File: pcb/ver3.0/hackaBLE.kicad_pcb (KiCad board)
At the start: 2 copper layers, 20.3 x 29.9 mm, 32 parts, among them J1 GPIO, J2 GPIO, J3 GPIO, J5 GPIO, J7 SWD, SW1 SW_Push, U1 nrf52832, U3 RF_Antenna, Y1 32.768KHz, Y2 32MHz

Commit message: still working on it alot of error still there.
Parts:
- moved C3 6.82 mm to (169.2, 123.4), turned to 90 degrees
- moved C4 4.31 mm to (169.2, 127.5), turned to -90 degrees
- moved SW1 4.17 mm to (180.2, 128.2)
- moved R1 2.36 mm to (174.2, 129.5)
- moved R3 1.45 mm to (180.4, 125.8)
- moved R2 1.35 mm to (180.4, 124.2)
- moved R4 1.25 mm to (180.4, 122.8)
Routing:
- net VDD: track 77.6 -> 68.1 mm
- net GND: track 55.5 -> 60.7 mm
- net /RESET: track 33.2 -> 29.3 mm
- net /GREEN: track 15.2 -> 13.2 mm
- net /P0.09: track 25.1 -> 26.2 mm
- net /BLUE: track 13.8 -> 12.6 mm
- net /P0.10: track 27.3 -> 28.2 mm
- net /RED: track 13.3 -> 13.9 mm
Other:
- board size 20.3 x 29.9 mm -> 24.2 x 29.9 mm

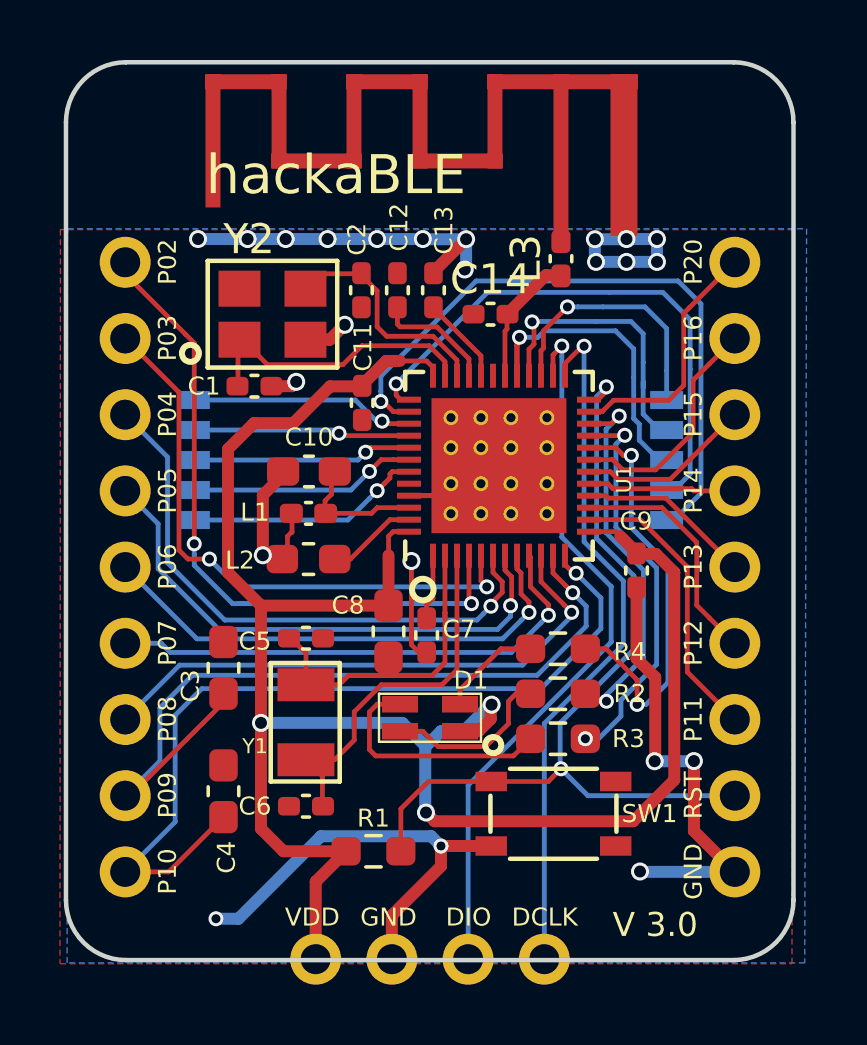
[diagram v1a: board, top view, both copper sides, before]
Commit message: now Version 3.0 has no Error and ready for manufacturing.
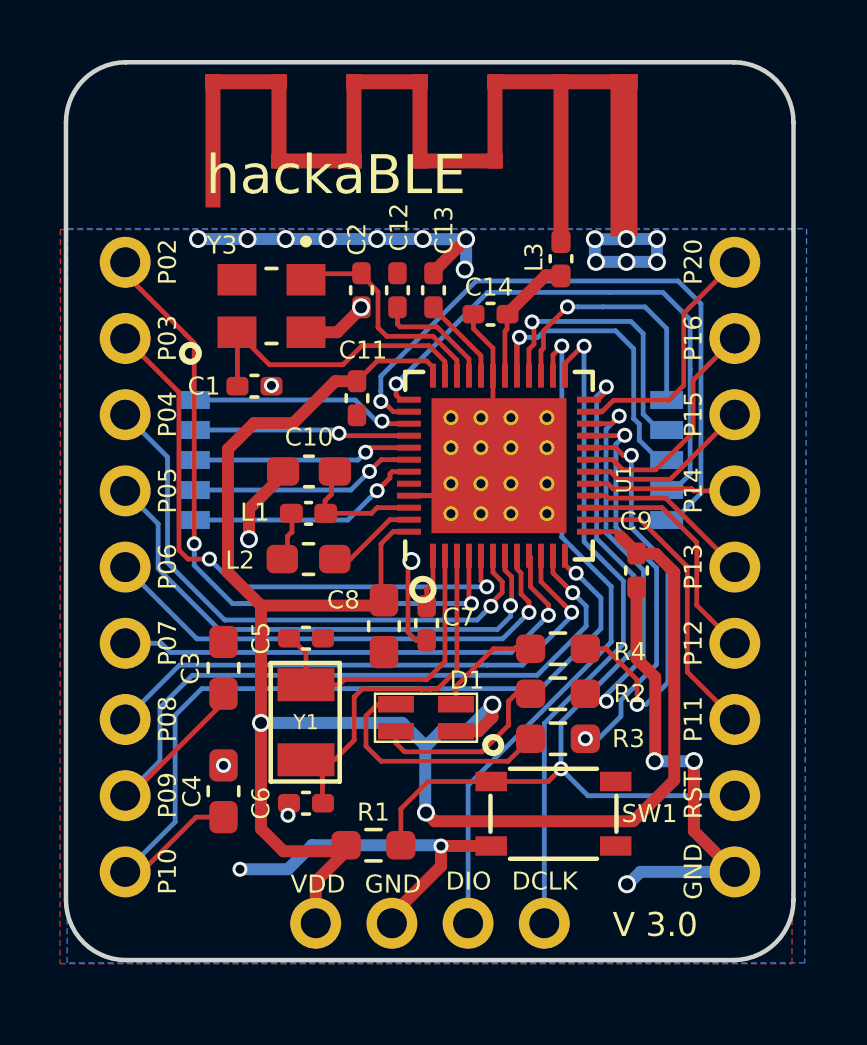
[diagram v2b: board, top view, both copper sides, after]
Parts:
- removed Y2: 32MHz, hackaBLE:32MHz_crystal
- added Y3: ABM8-32.000MHZ-B2-T3, crystal:XTAL_ABM8-32.000MHZ-B2-T3, F.Cu at (170.8, 111.3)
- moved J7 1.20 mm to (179.9, 131.9)
- moved C7 0.40 mm to (176.0, 121.9)
- moved C11 0.23 mm to (173.7, 114.4)
- moved C8 0.23 mm to (174.6, 122.0)
- moved R1 0.20 mm to (174.2, 129.3)
- moved D1 0.13 mm to (176.0, 125.0)
- moved C6 0.10 mm to (172.0, 127.9)
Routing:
- net /SWDIO: track 24.2 -> 23.0 mm
- net /SWDCLK: track 23.4 -> 22.2 mm
- net VDD: track 68.1 -> 67.5 mm
- net Net-(D1-BK): track 5.73 -> 6.28 mm
- net GND: track 60.7 -> 60.8 mm, vias 23 -> 25
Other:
- rule pad_to_mask_clearance: 0.2 -> 0.05
